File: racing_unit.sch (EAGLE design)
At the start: 71 parts, among them IC1 78M05, IC2 78M05, IC3 78M05, IC4 78M05, IC5 LM1117-3.3, IC6 ATMega328P-AU, Q1 IRFR120N, Q10 BC807, Q11 BC807, Q2 IRFR120N, Q3 IRFR120N, Q4 IRFR120N, Q5 BSS138, Q6 16MHz, Q8 BC807, Q9 BC807, X1 COIL1, X2 COIL2, X3 COIL3, X4 COIL4, X5 SUPPLY, X6 QS-SENSOR

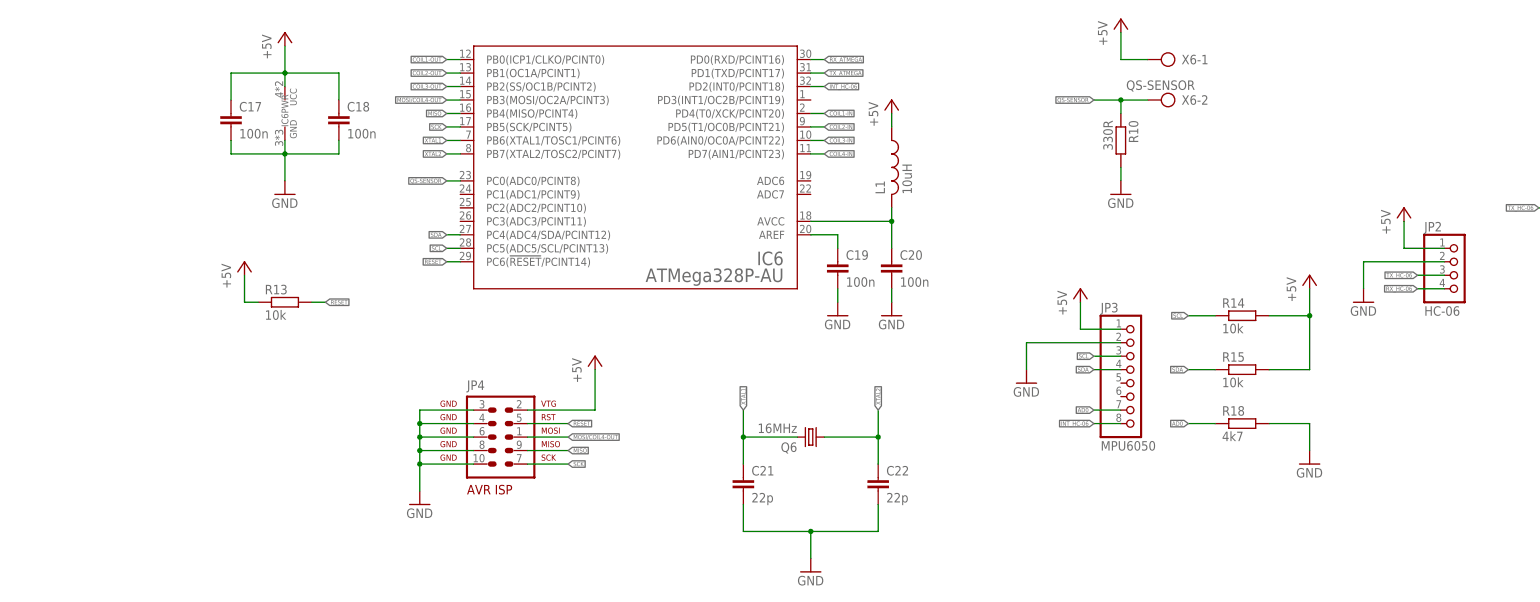
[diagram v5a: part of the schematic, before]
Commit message: fixed code warnings
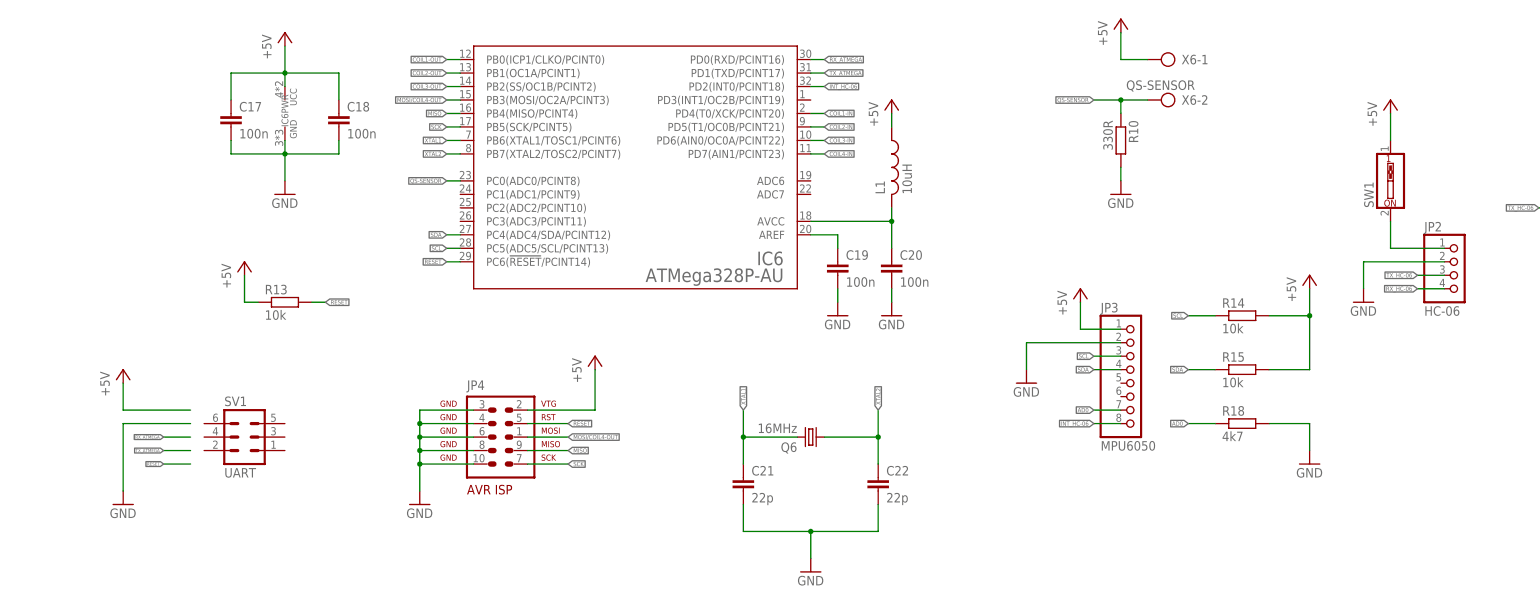
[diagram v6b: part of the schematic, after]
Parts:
- added SV1: UART, con-harting-ml:ML6
- added SW1: (no value), special:SW_DIP-1
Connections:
- new net N$20: JP2.1, SW1.2
- net +5V: now also SW1.1; no longer JP2.1
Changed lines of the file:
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@@
 <part name="P+19" library="supply1" deviceset="+5V" device=""/>
 <part name="P+20" library="supply1" deviceset="+5V" device=""/>
+<part name="SW1" library="special" deviceset="SW_DIP-1" device=""/>
+<part name="GND23" library="supply1" deviceset="GND" device=""/>
+<part name="P+21" library="supply1" deviceset="+5V" device=""/>
+<part name="SV1" library="con-harting-ml" deviceset="ML6" device="" value="UART"/>
 </parts>
 <sheets>
@@
 <instance part="JP2" gate="A" x="228.6" y="-40.64"/>
 <instance part="JP3" gate="A" x="167.64" y="-60.96"/>
-<instance part="P+13" gate="1" x="218.44" y="-27.94"/>
+<instance part="P+13" gate="1" x="215.9" y="-7.62"/>
 <instance part="P+16" gate="1" x="157.48" y="-43.18"/>
 <instance part="P+15" gate="1" x="200.66" y="-40.64"/>
@@
 <instance part="P+19" gate="1" x="35.56" y="58.42"/>
 <instance part="P+20" gate="1" x="-12.7" y="58.42"/>
+<instance part="SW1" gate="G$1" x="215.9" y="-22.86" rot="R90"/>
+<instance part="GND23" gate="1" x="-22.86" y="-83.82"/>
+<instance part="P+21" gate="1" x="-22.86" y="-58.42"/>
+<instance part="SV1" gate="1" x="0" y="-71.12"/>
 </instances>
 <busses>
@@
 <wire x1="256.54" y1="-53.34" x2="256.54" y2="-58.42" width="0.1524" layer="91"/>
 </segment>
+<segment>
+<wire x1="-15.24" y1="-73.66" x2="-10.16" y2="-73.66" width="0.1524" layer="91"/>
+<label x="-15.24" y="-73.66" size="0.6096" layer="95" rot="R180" xref="yes"/>
+</segment>
 </net>
 <net name="N$13" class="0">
@@
 <wire x1="12.7" y1="-45.72" x2="15.24" y2="-45.72" width="0.1524" layer="91"/>
 <label x="15.24" y="-45.72" size="0.8128" layer="95" xref="yes"/>
+</segment>
+<segment>
+<wire x1="-15.24" y1="-76.2" x2="-10.16" y2="-76.2" width="0.1524" layer="91"/>
+<label x="-15.24" y="-76.2" size="0.6096" layer="95" rot="R180" xref="yes"/>
 </segment>
 </net>
@@
 <junction x="269.24" y="-27.94"/>
 <pinref part="R12" gate="G$1" pin="1"/>
+</segment>
+<segment>
+<wire x1="-15.24" y1="-71.12" x2="-10.16" y2="-71.12" width="0.1524" layer="91"/>
+<label x="-15.24" y="-71.12" size="0.6096" layer="95" rot="R180" xref="yes"/>
 </segment>
 </net>
@@
 </segment>
 <segment>
-<pinref part="JP2" gate="A" pin="1"/>
-<wire x1="226.06" y1="-35.56" x2="218.44" y2="-35.56" width="0.1524" layer="91"/>
-<wire x1="218.44" y1="-35.56" x2="218.44" y2="-30.48" width="0.1524" layer="91"/>
-<pinref part="P+13" gate="1" pin="+5V"/>
-</segment>
-<segment>
 <pinref part="JP3" gate="A" pin="1"/>
 <wire x1="165.1" y1="-50.8" x2="157.48" y2="-50.8" width="0.1524" layer="91"/>
@@
 <wire x1="33.02" y1="50.8" x2="35.56" y2="50.8" width="0.1524" layer="91"/>
 <wire x1="35.56" y1="50.8" x2="35.56" y2="55.88" width="0.1524" layer="91"/>
+</segment>
+<segment>
+<pinref part="P+13" gate="1" pin="+5V"/>
+<pinref part="SW1" gate="G$1" pin="1"/>
+<wire x1="215.9" y1="-10.16" x2="215.9" y2="-15.24" width="0.1524" layer="91"/>
+</segment>
+<segment>
+<wire x1="-10.16" y1="-66.04" x2="-22.86" y2="-66.04" width="0.1524" layer="91"/>
+<wire x1="-22.86" y1="-66.04" x2="-22.86" y2="-60.96" width="0.1524" layer="91"/>
+<pinref part="P+21" gate="1" pin="+5V"/>
 </segment>
 </net>
@@
 <wire x1="256.54" y1="-88.9" x2="256.54" y2="-93.98" width="0.1524" layer="91"/>
 </segment>
+<segment>
+<pinref part="GND23" gate="1" pin="GND"/>
+<wire x1="-22.86" y1="-81.28" x2="-22.86" y2="-68.58" width="0.1524" layer="91"/>
+<wire x1="-22.86" y1="-68.58" x2="-10.16" y2="-68.58" width="0.1524" layer="91"/>
+</segment>
 </net>
 <net name="N$5" class="0">
@@
 </segment>
 </net>
+<net name="N$20" class="0">
+<segment>
+<pinref part="JP2" gate="A" pin="1"/>
+<wire x1="226.06" y1="-35.56" x2="215.9" y2="-35.56" width="0.1524" layer="91"/>
+<pinref part="SW1" gate="G$1" pin="2"/>
+<wire x1="215.9" y1="-35.56" x2="215.9" y2="-30.48" width="0.1524" layer="91"/>
+</segment>
+</net>

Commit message: updated schematic
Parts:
- removed C21, C22: 22p, rcl:C-EUC0805
- removed Q11: BC807, transistor-npn:BC817-16LT1SMD
- added C13, C14: 10u tantalum, rcl:CPOL-EUA/3216-18R
- added C15, C16: 100n, rcl:C-EUC0805
- added D5, D6, D7, D8: US1M, diode:DIODE-DO214AC
- added IC7: ATMega328P-AU, atmel_tiny24-44-84tiny48-88mega48-88-168-328:ATMEGA48/88/168/328-AU
- added Q7: BC807, transistor-npn:BC817-16LT1SMD
- C10: value 4700uF/25V -> 100n; device rcl:CPOL-EUE7.5-16 -> rcl:C-EUC0805
- C11, C12: value 10u tantalum -> 4700uF/25V; device rcl:CPOL-EUA/3216-18R -> rcl:CPOL-EUE7.5-16
- C19, C20: value 100n -> 22p
- C9: value 4700uF/25V -> 330n; device rcl:CPOL-EUE7.5-16 -> rcl:C-EUC0805
- IC5: value LM1117-3.3 -> 78M05; device v-reg-2:LM1117 -> v-reg-2:LM1117TO252
- IC6: value ATMega328P-AU -> LM1117-3.3; device atmel_tiny24-44-84tiny48-88mega48-88-168-328:ATMEGA48/88/168/328-AU -> v-reg-2:LM1117
- Q10: value BC807 -> 16MHz; device transistor-npn:BC817-16LT1SMD -> crystal:CRYSTALHC49S
- Q5: value BSS138 -> BC807; device m-pad-2.1:BSS138 -> transistor-npn:BC817-16LT1SMD
- Q6: value 16MHz -> BC807; device crystal:CRYSTALHC49S -> transistor-npn:BC817-16LT1SMD
- Q9: value BC807 -> BSS138; device transistor-npn:BC817-16LT1SMD -> m-pad-2.1:BSS138
- R1: value 150R -> 1k; device resistor:R-EU_0204/5 -> rcl:R-EU_M0805
- R10: value 330R -> 1k; device resistor:R-EU_0204/5 -> rcl:R-EU_M0805
- R11, R12: value 10k -> 1k
- R13: value 10k -> 150R; device rcl:R-EU_M0805 -> resistor:R-EU_0204/5
- R14: value 10k -> 330R; device rcl:R-EU_M0805 -> resistor:R-EU_0204/5
- R18: value 4k7 -> 10k
- R21: value 10k -> 4k7
- R5, R6, R7, R8: value 1k -> 10k
- SW1: value (none) -> BLUETOOTH
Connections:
- new net +12V: C9.1, D5.C, D6.C, D7.C, D8.C, IC5.IN
- new net N$21: C1.1, D1.C, IC1.IN
- new net N$22: C3.1, D2.C, IC2.IN
- new net N$23: C5.1, D3.C, IC3.IN
- new net N$24: C7.1, D4.C, IC4.IN
- new net N$25: C10.1, IC5.OUT
- net +3V3: now also C14.+, IC6.OUT, Q9.G, R15.2; no longer C12.+, IC5.OUT, Q5.G, R11.2
- net +5V: now also C12.+, C13.+, C15.1, C16.1, IC6.IN, IC7PWR.UCC, R16.2, R17.1, R18.2, R5.2, R6.2, R7.2, R8.2, SV1.5; no longer C10.+, C17.1, C18.1, C9.+, D1.C, D2.C, D3.C, D4.C, IC5.IN, IC6PWR.UCC, R1.1, R12.2, R14.2, R15.2, R20.2, R21.2, R22.2
- net AD0: now also R21.1; no longer R18.1
- net COIL1-IN: now also IC7IC.PD4(T0/XCK/PCINT20), R1.2; no longer IC6IC.PD4(T0/XCK/PCINT20), R3.2
- net COIL1-OUT: now also IC7IC.PB0(ICP1/CLKO/PCINT0), R9.1; no longer IC6IC.PB0(ICP1/CLKO/PCINT0), R2.1
- net COIL2-IN: now also IC7IC.PD5(T1/OC0B/PCINT21), R2.2; no longer IC6IC.PD5(T1/OC0B/PCINT21), R5.2
- net COIL2-OUT: now also IC7IC.PB1(OC1A/PCINT1), R10.1; no longer IC6IC.PB1(OC1A/PCINT1), R4.1
- net COIL3-IN: now also IC7IC.PD6(AIN0/OC0A/PCINT22), R3.2; no longer IC6IC.PD6(AIN0/OC0A/PCINT22), R7.2
- net COIL3-OUT: now also IC7IC.PB2(SS/OC1B/PCINT2), R11.1; no longer IC6IC.PB2(SS/OC1B/PCINT2), R6.1
- net COIL4-IN: now also IC7IC.PD7(AIN1/PCINT23), R4.2; no longer IC6IC.PD7(AIN1/PCINT23), R9.2
- net GND: now also C10.2, C13.-, C14.-, C15.2, C16.2, C9.2, IC6.GND, IC7PWR.GND, Q5.E, Q6.E, Q7.E, R14.1, R21.2, R22.1, SV1.1, SV1.3; no longer C10.-, C21.2, C22.2, C9.-, IC6PWR.GND, Q10.E, Q11.E, Q9.E, R10.2, R16.1, R18.2
- net INT_HC-06: now also IC7IC.PD2(INT0/PCINT18); no longer IC6IC.PD2(INT0/PCINT18)
- net MISO: now also IC7IC.PB4(MISO/PCINT4); no longer IC6IC.PB4(MISO/PCINT4)
- net MOSI/COIL4-OUT: now also IC7IC.PB3(MOSI/OC2A/PCINT3), R12.1; no longer IC6IC.PB3(MOSI/OC2A/PCINT3), R8.1
- net N$1: now also D1.A, D5.A; no longer C1.1, IC1.IN
- net N$123: now also Q5.C, R5.1; no longer Q8.C, R19.1
- net N$124: now also Q6.C, R6.1; no longer Q9.C, R20.1
- net N$125: now also Q7.C, R7.1; no longer Q10.C, R21.1
- net N$126: now also Q8.C, R8.1; no longer Q11.C, R22.1
- net N$13: now also R13.2; no longer R1.2
- net N$14: now also R1.1; no longer D1.A, R3.1
- net N$15: now also R2.1; no longer D2.A, R5.1
- net N$16: now also Q7.B, R11.2; no longer Q10.B, R6.2
- net N$17: now also R4.1; no longer D4.A, R9.1
- net N$18: now also R3.1; no longer D3.A, R7.1
- net N$19: now also Q8.B, R12.2; no longer Q11.B, R8.2
- net N$2: now also D2.A, D6.A; no longer C3.1, IC2.IN
- net N$3: now also D3.A, D7.A; no longer C5.1, IC3.IN
- net N$4: now also D4.A, D8.A; no longer C7.1, IC4.IN
- net N$5: now also C17.1, IC7IC.AREF; no longer C19.1, IC6IC.AREF
- net N$6: now also C18.1, IC7IC.AVCC; no longer C20.1, IC6IC.AVCC
- net N$7: now also Q5.B, R9.2; no longer Q8.B, R2.2
- net N$8: now also Q6.B, R10.2; no longer Q9.B, R4.2
- net QS-SENSOR: now also IC7IC.PC0(ADC0/PCINT8), R14.2; no longer IC6IC.PC0(ADC0/PCINT8), R10.1
- net RESET: now also IC7IC.PC6(!RESET!/PCINT14), R17.2, SV1.6; no longer IC6IC.PC6(!RESET!/PCINT14), R13.2
- net RX_ATMEGA: now also IC7IC.PD0(RXD/PCINT16), Q9.D, R16.1, SV1.2; no longer IC6IC.PD0(RXD/PCINT16), Q5.D, R12.1
- net RX_HC-06: now also R20.1, R22.2; no longer R16.2, R17.1
- net SCK: now also IC7IC.PB5(SCK/PCINT5); no longer IC6IC.PB5(SCK/PCINT5)
- net SCL: now also IC7IC.PC5(ADC5/SCL/PCINT13), R18.1; no longer IC6IC.PC5(ADC5/SCL/PCINT13), R14.1
- net SDA: now also IC7IC.PC4(ADC4/SDA/PCINT12), R19.1; no longer IC6IC.PC4(ADC4/SDA/PCINT12), R15.1
- net TX_ATMEGA: now also IC7IC.PD1(TXD/PCINT17), R20.2, SV1.4; no longer IC6IC.PD1(TXD/PCINT17), R17.2
- net TX_HC-06: now also Q9.S, R15.1; no longer Q5.S, R11.1
- net XTAL1: now also C19.1, IC7IC.PB6(XTAL1/TOSC1/PCINT6), Q10.2; no longer C21.1, IC6IC.PB6(XTAL1/TOSC1/PCINT6), Q6.2
- net XTAL2: now also C20.1, IC7IC.PB7(XTAL2/TOSC2/PCINT7), Q10.1; no longer C22.1, IC6IC.PB7(XTAL2/TOSC2/PCINT7), Q6.1
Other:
- moved on the sheet: C1, C11, C12, C17, C18, C19, C2, C20, C3, C4, C5, C6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

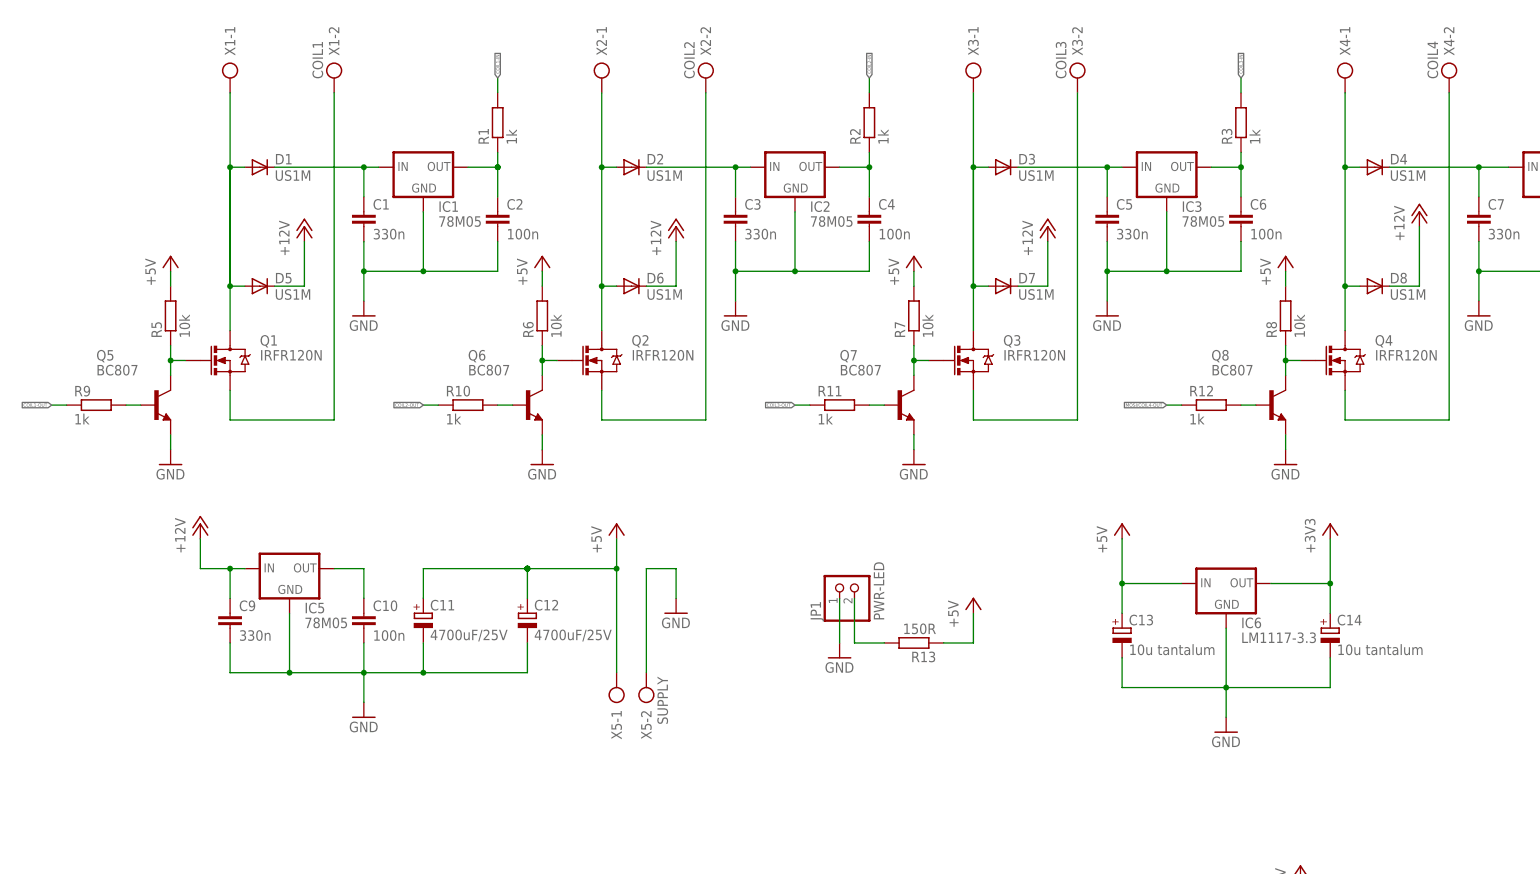
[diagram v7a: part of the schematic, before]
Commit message: removed +12v supply from coils
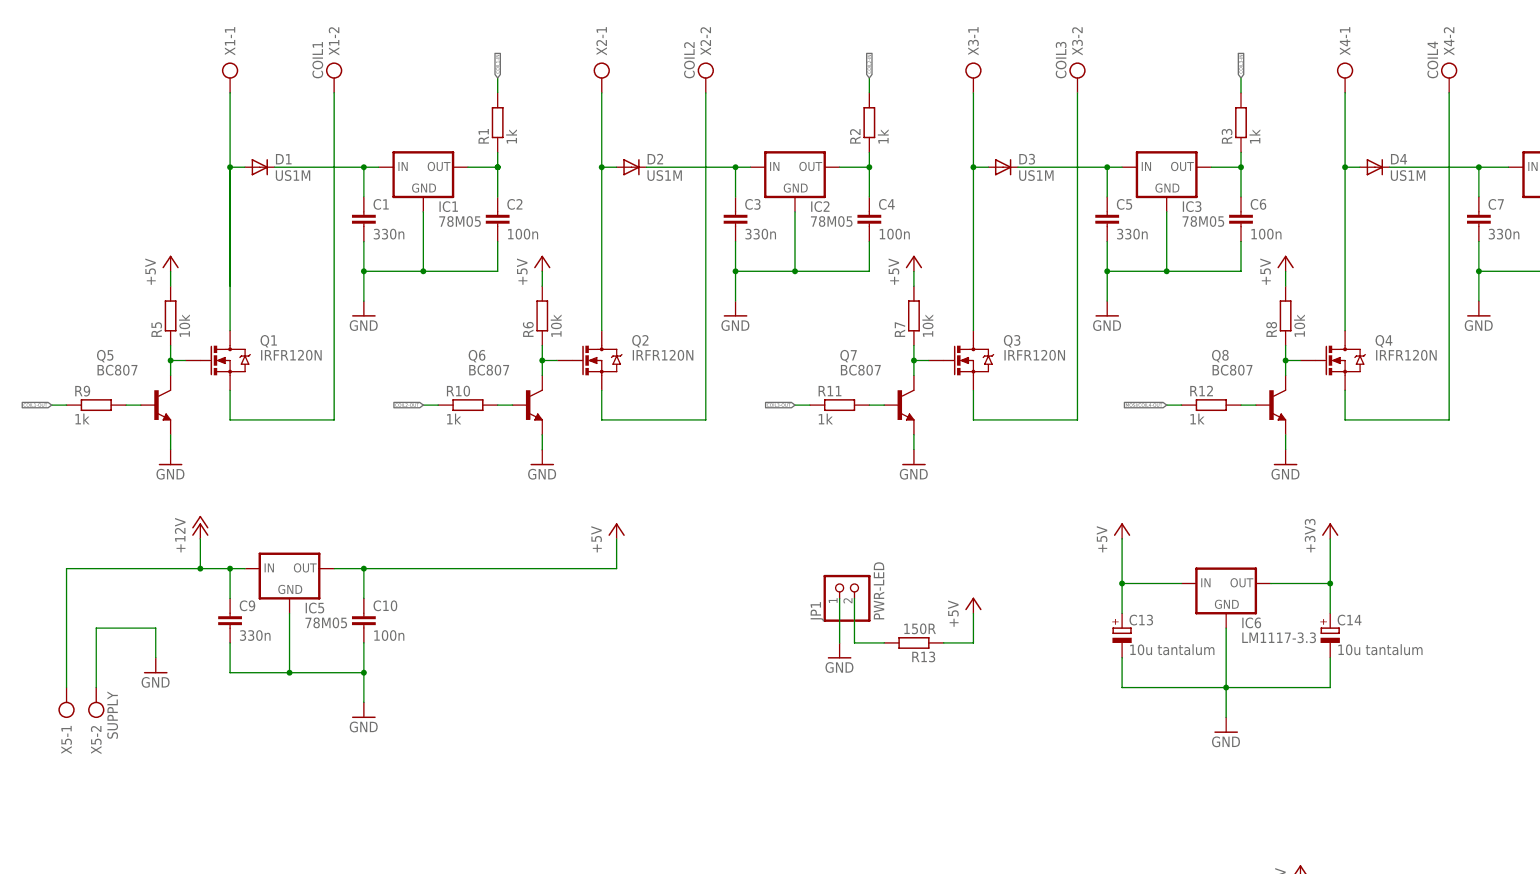
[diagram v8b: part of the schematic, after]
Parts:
- removed C11, C12: 4700uF/25V, rcl:CPOL-EUE7.5-16
- removed D5, D6, D7, D8: US1M, diode:DIODE-DO214AC
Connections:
- removed net N$25: C10.1, IC5.OUT
- net +12V: now also X5-1.KL; no longer D5.C, D6.C, D7.C, D8.C
- net +5V: now also C10.1, IC5.OUT; no longer C11.+, C12.+, X5-1.KL
- net GND: no longer C11.-, C12.-
- net N$1: no longer D5.A
- net N$2: no longer D6.A
- net N$3: no longer D7.A
- net N$4: no longer D8.A
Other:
- moved on the sheet: X5-1, X5-2
